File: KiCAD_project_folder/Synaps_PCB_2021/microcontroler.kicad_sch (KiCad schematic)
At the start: 35 parts, among them IC2 ESP32-S2, SW3 SW_Push, SW4 SW_Push, U3 AT25DF041x-UxN-x, Y2 Crystal_GND24, Y3 32.768K

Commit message: Updated pcb editor with the new components imported
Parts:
- C10, C11, C2, C3, C4, C5, C6, C7, C8: footprint (none) -> Capacitor_SMD:C_1206_3216Metric_Pad1.33x1.80mm_HandSolder
- R13, R14, R15, R16, R17, R18, R6, R7, R8: footprint (none) -> Resistor_SMD:R_1206_3216Metric_Pad1.30x1.75mm_HandSolder
- SW3, SW4: footprint (none) -> Button_Switch_SMD:SW_Push_1P1T_NO_6x6mm_H9.5mm
- Y2, Y3: footprint (none) -> Crystal:Crystal_SMD_0603-2Pin_6.0x3.5mm_HandSoldering
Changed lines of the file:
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@@
     (property "Reference" "SW4" (id 0) (at 129.54 176.53 0))
     (property "Value" "SW_Push" (id 1) (at 138.43 176.53 0))
-    (property "Footprint" "" (id 2) (at 133.35 175.26 0)
+    (property "Footprint" "Button_Switch_SMD:SW_Push_1P1T_NO_6x6mm_H9.5mm" (id 2) (at 133.35 175.26 0)
       (effects (font (size 1.27 1.27)) hide)
     )
@@
     (property "Reference" "C8" (id 0) (at 24.13 168.91 90))
     (property "Value" "12.5pF" (id 1) (at 33.02 168.91 90))
-    (property "Footprint" "" (id 2) (at 31.75 166.6748 0)
+    (property "Footprint" "Capacitor_SMD:C_1206_3216Metric_Pad1.33x1.80mm_HandSolder" (id 2) (at 31.75 166.6748 0)
       (effects (font (size 1.27 1.27)) hide)
     )
@@
       (effects (font (size 1.27 1.27)) (justify left))
     )
-    (property "Footprint" "" (id 2) (at 103.8352 46.99 0)
+    (property "Footprint" "Capacitor_SMD:C_1206_3216Metric_Pad1.33x1.80mm_HandSolder" (id 2) (at 103.8352 46.99 0)
       (effects (font (size 1.27 1.27)) hide)
     )
@@
     (property "Reference" "C10" (id 0) (at 87.63 184.15 90))
     (property "Value" "0.1uF/50V(10%)(NC)" (id 1) (at 95.25 189.23 90))
-    (property "Footprint" "" (id 2) (at 87.63 186.3852 0)
+    (property "Footprint" "Capacitor_SMD:C_1206_3216Metric_Pad1.33x1.80mm_HandSolder" (id 2) (at 87.63 186.3852 0)
       (effects (font (size 1.27 1.27)) hide)
     )
@@
     (property "Reference" "R16" (id 0) (at 250.19 24.6212 90))
     (property "Value" "0" (id 1) (at 250.19 27.1581 90))
-    (property "Footprint" "" (id 2) (at 250.444 28.194 90)
+    (property "Footprint" "Resistor_SMD:R_1206_3216Metric_Pad1.30x1.75mm_HandSolder" (id 2) (at 250.444 28.194 90)
       (effects (font (size 1.27 1.27)) hide)
     )
@@
     (property "Reference" "C7" (id 0) (at 24.13 152.4 90))
     (property "Value" "12.5pF" (id 1) (at 33.02 152.4 90))
-    (property "Footprint" "" (id 2) (at 31.75 154.6352 0)
+    (property "Footprint" "Capacitor_SMD:C_1206_3216Metric_Pad1.33x1.80mm_HandSolder" (id 2) (at 31.75 154.6352 0)
       (effects (font (size 1.27 1.27)) hide)
     )
@@
       (effects (font (size 1.27 1.27)) (justify left))
     )
-    (property "Footprint" "" (id 2) (at 155.2448 46.99 0)
+    (property "Footprint" "Capacitor_SMD:C_1206_3216Metric_Pad1.33x1.80mm_HandSolder" (id 2) (at 155.2448 46.99 0)
       (effects (font (size 1.27 1.27)) hide)
     )
@@
     (property "Reference" "R7" (id 0) (at 185.42 116.84 90))
     (property "Value" "0" (id 1) (at 195.58 116.84 90))
-    (property "Footprint" "" (id 2) (at 190.754 117.094 90)
+    (property "Footprint" "Resistor_SMD:R_1206_3216Metric_Pad1.30x1.75mm_HandSolder" (id 2) (at 190.754 117.094 90)
       (effects (font (size 1.27 1.27)) hide)
     )
@@
     (property "Reference" "R8" (id 0) (at 185.42 119.38 90))
     (property "Value" "0" (id 1) (at 195.58 119.38 90))
-    (property "Footprint" "" (id 2) (at 190.754 119.634 90)
+    (property "Footprint" "Resistor_SMD:R_1206_3216Metric_Pad1.30x1.75mm_HandSolder" (id 2) (at 190.754 119.634 90)
       (effects (font (size 1.27 1.27)) hide)
     )
@@
     (property "Reference" "C11" (id 0) (at 129.54 184.15 90))
     (property "Value" "0.1uF/50V(10%)(NC)" (id 1) (at 137.16 189.23 90))
-    (property "Footprint" "" (id 2) (at 129.54 186.3852 0)
+    (property "Footprint" "Capacitor_SMD:C_1206_3216Metric_Pad1.33x1.80mm_HandSolder" (id 2) (at 129.54 186.3852 0)
       (effects (font (size 1.27 1.27)) hide)
     )
@@
       (effects (font (size 1.27 1.27)) (justify left))
     )
-    (property "Footprint" "" (id 2) (at 171.1452 26.67 0)
+    (property "Footprint" "Capacitor_SMD:C_1206_3216Metric_Pad1.33x1.80mm_HandSolder" (id 2) (at 171.1452 26.67 0)
       (effects (font (size 1.27 1.27)) hide)
     )
@@
     (property "Reference" "SW3" (id 0) (at 87.63 176.53 0))
     (property "Value" "SW_Push" (id 1) (at 96.52 176.53 0))
-    (property "Footprint" "" (id 2) (at 91.44 175.26 0)
+    (property "Footprint" "Button_Switch_SMD:SW_Push_1P1T_NO_6x6mm_H9.5mm" (id 2) (at 91.44 175.26 0)
       (effects (font (size 1.27 1.27)) hide)
     )
@@
       (effects (font (size 1.27 1.27)) (justify left))
     )
-    (property "Footprint" "" (id 2) (at 183.8452 26.67 0)
+    (property "Footprint" "Capacitor_SMD:C_1206_3216Metric_Pad1.33x1.80mm_HandSolder" (id 2) (at 183.8452 26.67 0)
       (effects (font (size 1.27 1.27)) hide)
     )
@@
     (property "Reference" "R15" (id 0) (at 185.42 129.54 90))
     (property "Value" "0" (id 1) (at 195.58 129.54 90))
-    (property "Footprint" "" (id 2) (at 190.754 129.794 90)
+    (property "Footprint" "Resistor_SMD:R_1206_3216Metric_Pad1.30x1.75mm_HandSolder" (id 2) (at 190.754 129.794 90)
       (effects (font (size 1.27 1.27)) hide)
     )
@@
     (property "Reference" "R17" (id 0) (at 184.15 86.36 90))
     (property "Value" "499" (id 1) (at 194.31 86.36 90))
-    (property "Footprint" "" (id 2) (at 189.484 86.614 90)
+    (property "Footprint" "Resistor_SMD:R_1206_3216Metric_Pad1.30x1.75mm_HandSolder" (id 2) (at 189.484 86.614 90)
       (effects (font (size 1.27 1.27)) hide)
     )
@@
     (property "Reference" "R14" (id 0) (at 185.42 127 90))
     (property "Value" "0" (id 1) (at 195.58 127 90))
-    (property "Footprint" "" (id 2) (at 190.754 127.254 90)
+    (property "Footprint" "Resistor_SMD:R_1206_3216Metric_Pad1.30x1.75mm_HandSolder" (id 2) (at 190.754 127.254 90)
       (effects (font (size 1.27 1.27)) hide)
     )
@@
       (effects (font (size 1.27 1.27)) (justify right))
     )
-    (property "Footprint" "" (id 2) (at 42.164 160.274 90)
+    (property "Footprint" "Resistor_SMD:R_1206_3216Metric_Pad1.30x1.75mm_HandSolder" (id 2) (at 42.164 160.274 90)
       (effects (font (size 1.27 1.27)) hide)
     )
@@
       (effects (font (size 1.27 1.27)) (justify left))
     )
-    (property "Footprint" "" (id 2) (at 94.996 127.254 90)
+    (property "Footprint" "Resistor_SMD:R_1206_3216Metric_Pad1.30x1.75mm_HandSolder" (id 2) (at 94.996 127.254 90)
       (effects (font (size 1.27 1.27)) hide)
     )
@@
       (effects (font (size 1.27 1.27)) (justify left))
     )
-    (property "Footprint" "" (id 2) (at 131.7752 46.99 0)
+    (property "Footprint" "Capacitor_SMD:C_1206_3216Metric_Pad1.33x1.80mm_HandSolder" (id 2) (at 131.7752 46.99 0)
       (effects (font (size 1.27 1.27)) hide)
     )
@@
       (effects (font (size 1.27 1.27)) hide)
     )
-    (property "Footprint" "" (id 2) (at 259.08 35.56 0)
+    (property "Footprint" "Crystal:Crystal_SMD_0603-2Pin_6.0x3.5mm_HandSoldering" (id 2) (at 259.08 35.56 0)
       (effects (font (size 1.27 1.27)) hide)
     )
@@
     (property "Reference" "R13" (id 0) (at 185.42 121.92 90))
     (property "Value" "0" (id 1) (at 195.58 121.92 90))
-    (property "Footprint" "" (id 2) (at 190.754 122.174 90)
+    (property "Footprint" "Resistor_SMD:R_1206_3216Metric_Pad1.30x1.75mm_HandSolder" (id 2) (at 190.754 122.174 90)
       (effects (font (size 1.27 1.27)) hide)
     )
@@
       (effects (font (size 1.27 1.27)) (justify left))
     )
-    (property "Footprint" "" (id 2) (at 35.56 160.02 0)
-      (effects (font (size 1.27 1.27)) hide)
-    )
+    (property "Footprint" "Crystal:Crystal_SMD_0603-2Pin_6.0x3.5mm_HandSoldering" (id 2) (at 35.56 160.02 0)
+      (effects (font (size 1.27 1.27)) hide)
+    )

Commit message: Update schematic sheets and creates image to allow the board setup to be shared
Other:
- company: (none) -> Club SynapsÉTS
- title: (none) -> Misca PCB
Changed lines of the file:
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@@
 (kicad_sch (version 20211123) (generator eeschema)
   (paper "A4")
+  (title_block
+    (title "Misca PCB")
+    (date "2022-06-17")
+    (rev "A2")
+    (company "Club SynapsÉTS")
+    (comment 1 "Auteur : Jacques Veneziano")
+  )
   (junction (at 97.79 180.34) (diameter 0) (color 0 0 0 0)
   )

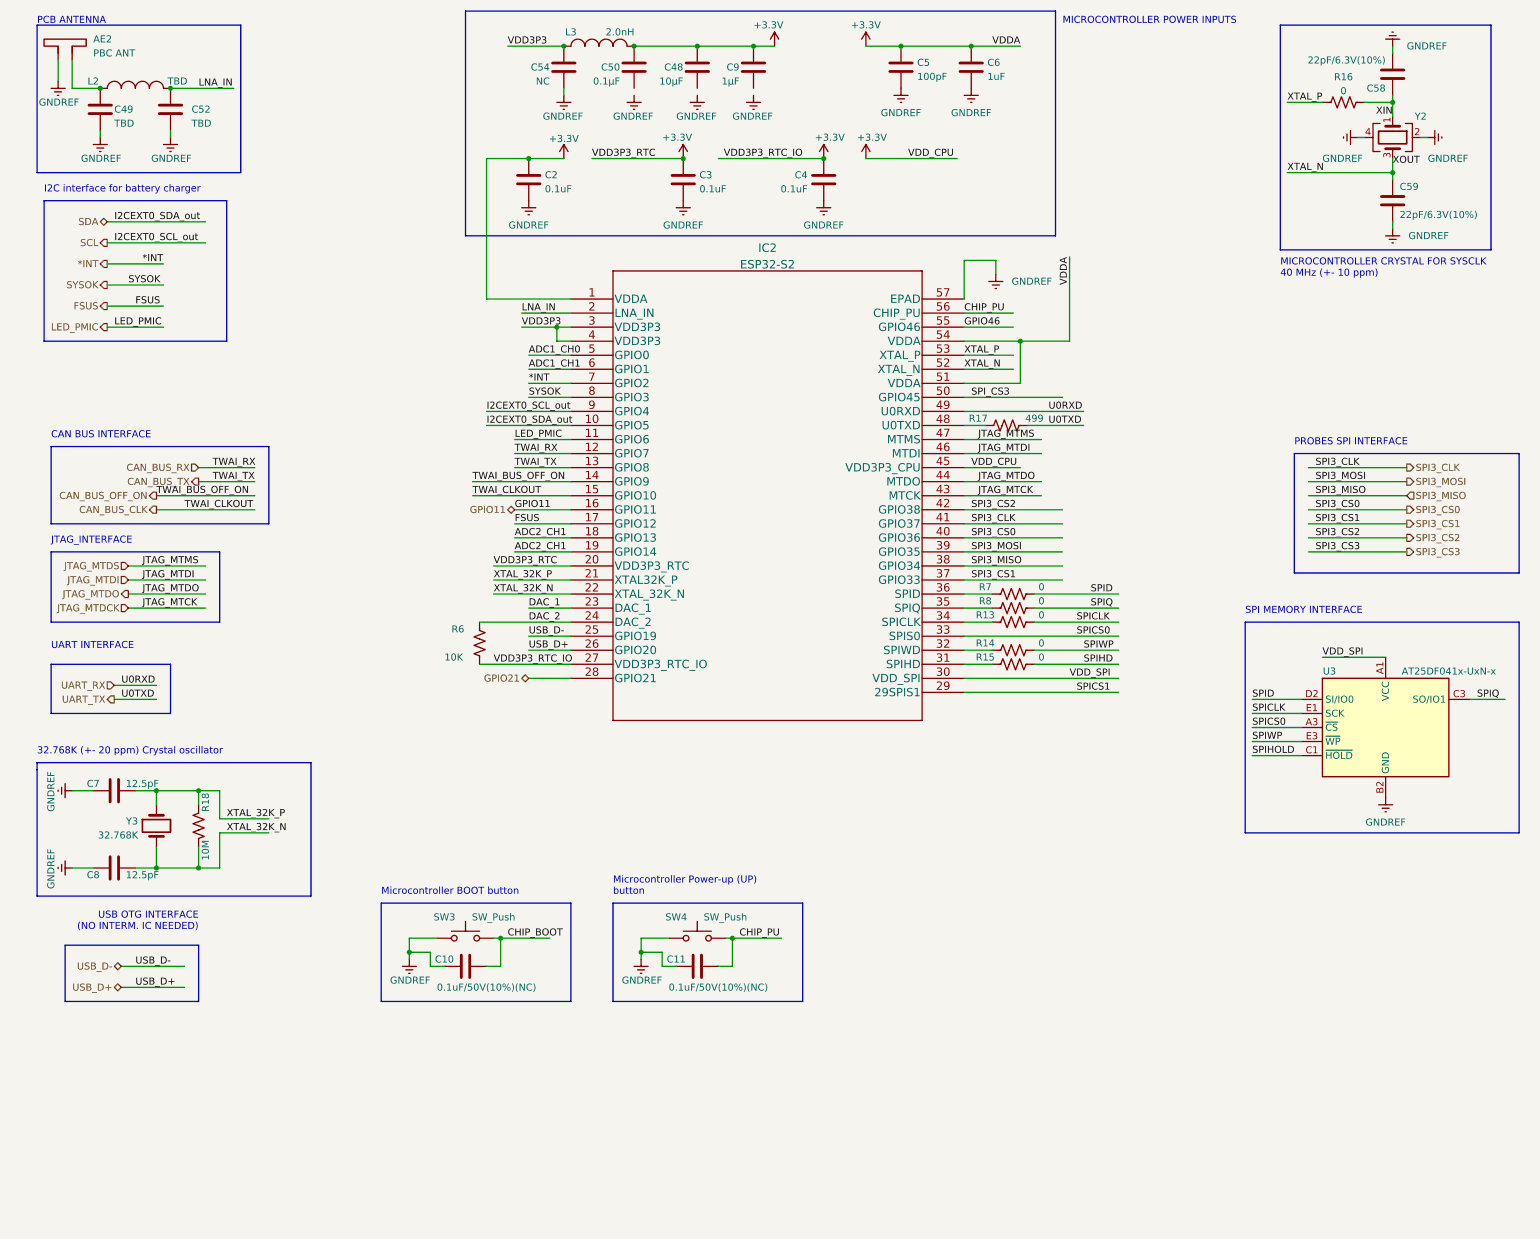
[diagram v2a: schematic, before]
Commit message: Updated BOM and power circuit has to be redone because of missing parts
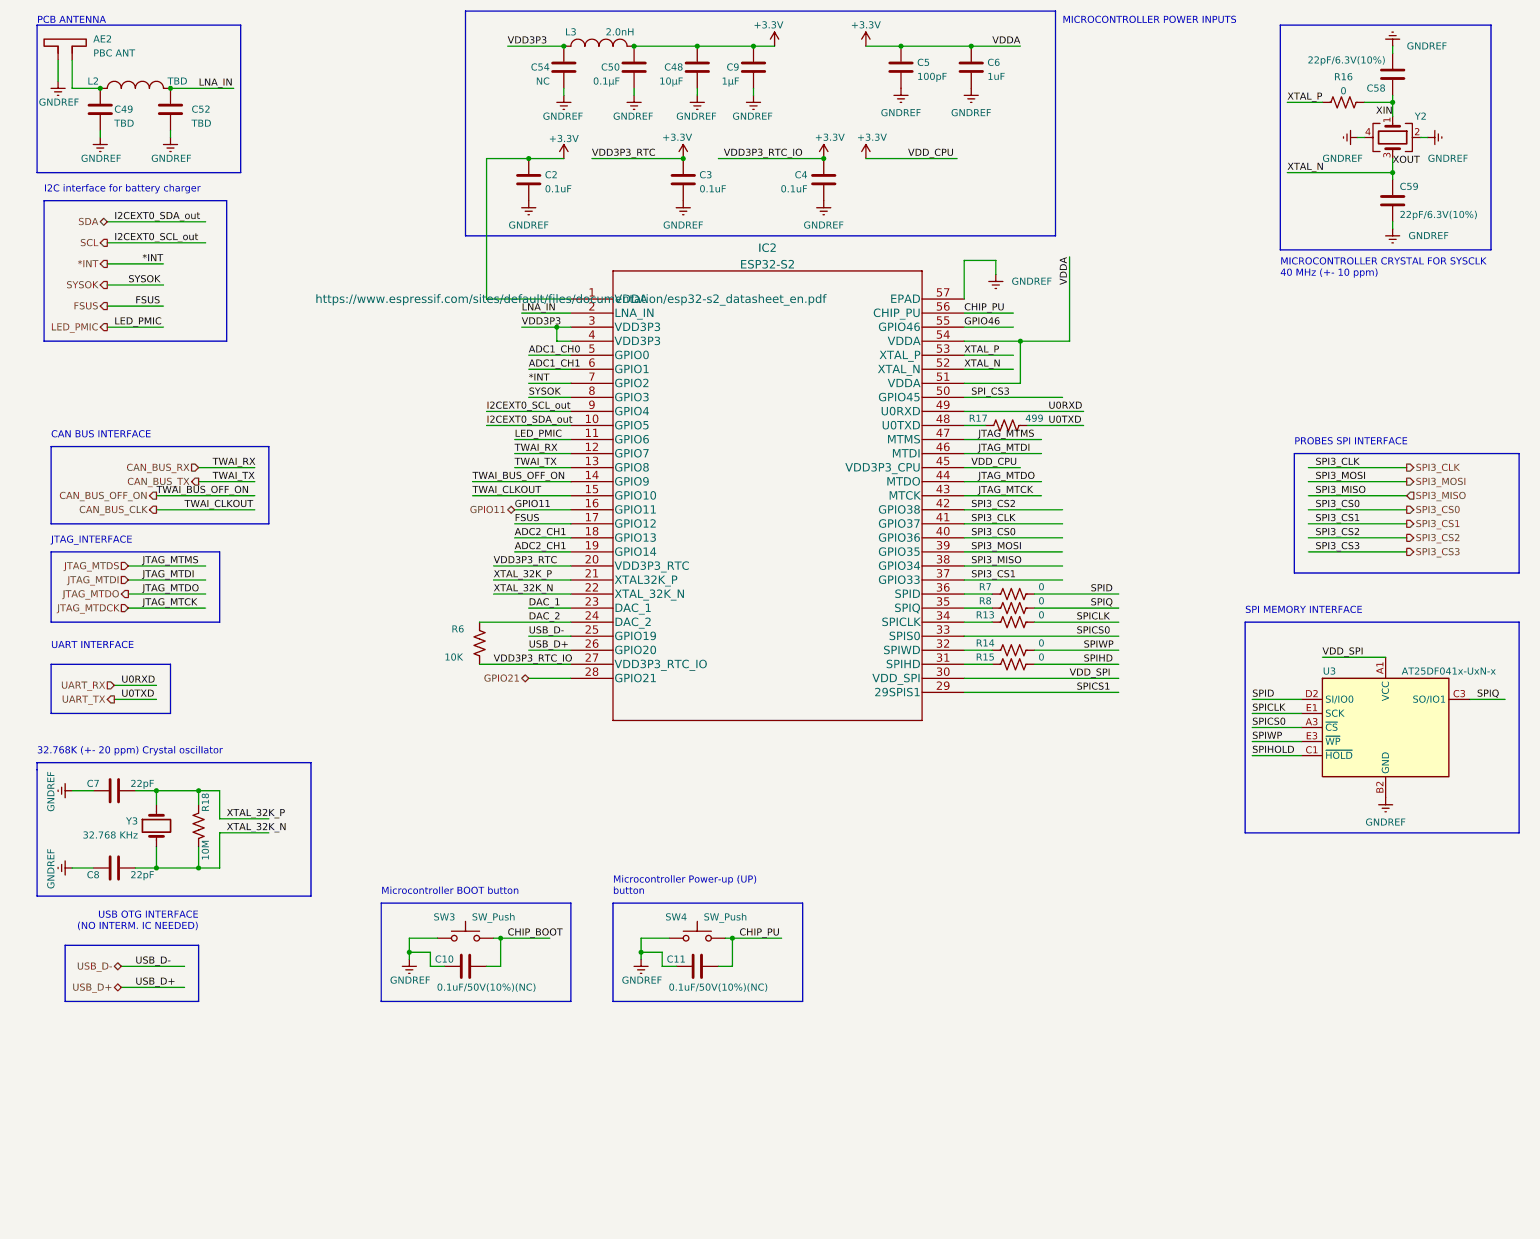
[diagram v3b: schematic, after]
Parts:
- C10, C11, C2, C3, C4, C50: MPN (none) -> CC1206KRX7R9BB104; Supplier Link (none) -> https://www.digikey.ca/en/products/detail/yageo/CC1206KRX7R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
- C48: MPN (none) -> CL31B106KAHNNNE; Supplier Link (none) -> https://www.digikey.ca/en/products/detail/samsung-electro-m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
- C5: MPN (none) -> GRM31A7U3A101JW31D; Supplier Link (none) -> https://www.digikey.ca/en/products/detail/murata-electronic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
- C58, C59: MPN (none) -> CL31C220JBCNNNC; Supplier Link (none) -> https://www.digikey.ca/en/products/detail/samsung-electro-m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
- C6, C9: MPN (none) -> GCM31MR71H105KA55L; Supplier Link (none) -> https://www.digikey.ca/en/products/detail/murata-electronic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
- C7, C8: value 12.5pF -> 22pF; MPN (none) -> CL31C220JBCNNNC; Supplier Link (none) -> https://www.digikey.ca/en/products/detail/samsung-electro-m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
- IC2: MPN (none) -> ESP32-S2FN4R2; Supplier Link (none) -> https://www.digikey.ca/en/products/detail/espressif-systems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
- R13, R14, R15, R16, R7, R8: MPN (none) -> RC1206JR-070RL; Supplier Link (none) -> https://www.digikey.ca/en/products/detail/yageo/RC1206JR-07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
- R17: MPN (none) -> RC1206FR-07499RL; Supplier Link (none) -> https://www.digikey.ca/en/products/detail/yageo/RC1206FR-07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
- R18: MPN (none) -> RC1206FR-0710ML; Supplier Link (none) -> https://www.digikey.ca/en/products/detail/yageo/RC1206FR-07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
- R6: MPN (none) -> RC1206JR-0710KL; Supplier Link (none) -> https://www.digikey.ca/en/products/detail/yageo/RC1206JR-07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
- SW3, SW4: footprint Button_Switch_SMD:SW_Push_1P1T_NO_6x6mm_H9.5mm -> Push_Button:GPTS203211B; MPN (none) -> GPTS203211B; Supplier Link (none) -> https://www.digikey.ca/en/products/detail/cw-industries/GPT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
- Y2: value Crystal_GND24 -> 40 MHz; MPN (none) -> ECS-400-18-33-JGN-TR3; Supplier Link (none) -> https://www.digikey.ca/en/products/detail/ecs-inc/ECS-400-1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
- Y3: value 32.768K -> 32.768 KHz; MPN (none) -> ABS07-32.768KHZ-T; Supplier Link (none) -> https://www.digikey.ca/en/products/detail/abracon-llc/ABS07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
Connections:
- net GNDREF: now also C48.2, C50.2, C9.2

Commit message: schematic finished
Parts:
- C49: value TBD -> 19pF; footprint Capacitor_SMD:C_1206_3216Metric_Pad1.33x1.80mm_HandSolder -> Capacitor_SMD:C_01005_0402Metric; MPN (none) -> GCQ1555C1H190JB01D; Supplier Link (none) -> https://www.digikey.ca/en/products/detail/murata-electronic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
- C52: value TBD -> 16pF; footprint Capacitor_SMD:C_1206_3216Metric_Pad1.33x1.80mm_HandSolder -> Capacitor_SMD:C_01005_0402Metric_Pad0.57x0.30mm_HandSolder; MPN (none) -> GRM1555C1H160JA01D; Supplier Link (none) -> https://www.digikey.ca/en/products/detail/murata-electronic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
- L2: value TBD -> 0.5028nH
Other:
- note added: "Calculated perfect impedance values for pi type matching network L = 0.5028 nH CS = 15.915 pF CL - 19.347 pF"
- note added: "Restrictions because of ADC VDD = 3 V, fSCLK = 16 MHz => SPI_CLK = 16 MHz"

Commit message: Schematic update
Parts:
- C48: value 10µF -> 10uF
- C50: value 0.1µF -> 0.1uF
- C9: value 1µF -> 1uF
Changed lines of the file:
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@@
       (effects (font (size 1.27 1.27)) (justify left))
     )
-    (property "Value" "0.1µF" (at 119.38 25.4 0)
+    (property "Value" "0.1uF" (at 119.38 25.4 0)
       (effects (font (size 1.27 1.27)) (justify left))
     )
@@
       (effects (font (size 1.27 1.27)) (justify left))
     )
-    (property "Value" "1µF" (at 140.97 25.4 0)
+    (property "Value" "1uF" (at 140.97 25.4 0)
       (effects (font (size 1.27 1.27)) (justify left))
     )
@@
       (effects (font (size 1.27 1.27)) (justify left))
     )
-    (property "Value" "10µF" (at 130.81 25.4 0)
+    (property "Value" "10uF" (at 130.81 25.4 0)
       (effects (font (size 1.27 1.27)) (justify left))
     )
@@
       (effects (font (size 1.27 1.27)) hide)
     )
-    (property "Datasheet" "https://media.digikey.com/pdf/Data%20Sheets/Samsung%20PDFs/CL31B106KAHNNNE_Spec.pdf " (at 133.35 22.86 0)
-      (effects (font (size 1.27 1.27)) hide)
-    )
+    (property "Datasheet" "https://media.digikey.com/pdf/Data%20Sheets/Samsung%20PDFs/CL31B106KAHNNNE_Spec.pdf" (at 133.35 22.86 0)
+      (effects (font (size 1.27 1.27)) hide)
+    )
